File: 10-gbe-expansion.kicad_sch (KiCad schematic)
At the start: 4 parts

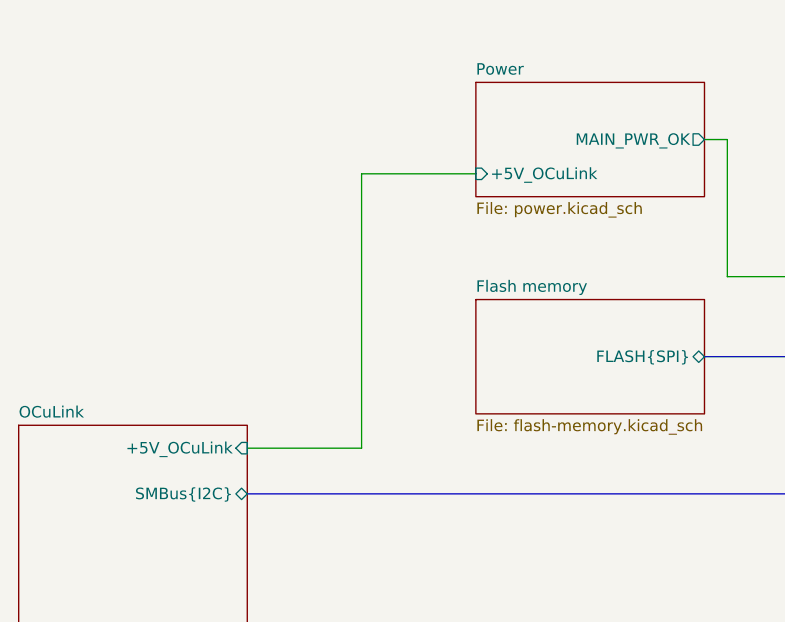
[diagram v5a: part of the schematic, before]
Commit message: [#80813] Remove OCuLink power pins connections
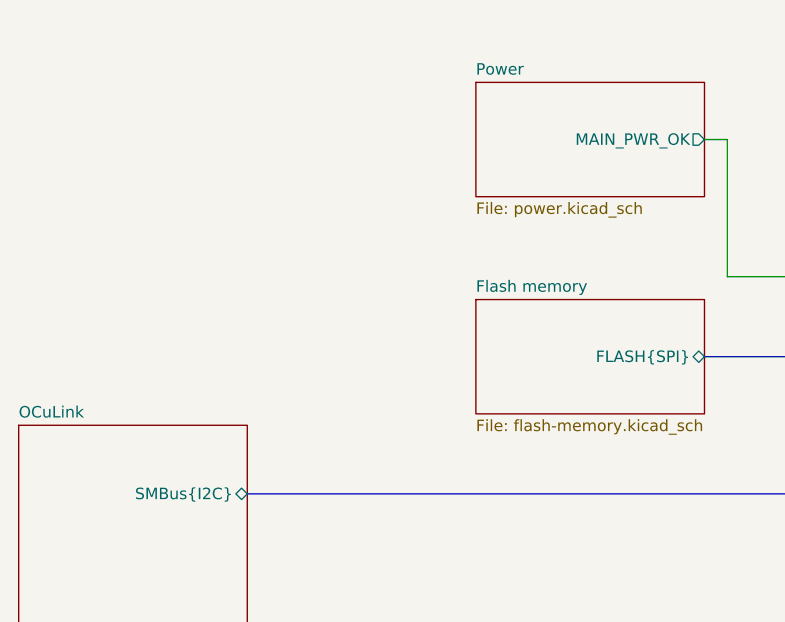
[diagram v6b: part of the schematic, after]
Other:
- sheet OCuLink ports: added none; removed +5V_OCuLink
- sheet Power ports: added none; removed +5V_OCuLink
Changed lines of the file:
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@@
-		)
-	)
-	(wire
-		(pts
-			(xy 88.9 99.06) (xy 88.9 129.54)
-		)
-		(stroke
-			(width 0)
-			(type default)
 		)
 	)
@@
 	(wire
 		(pts
-			(xy 101.6 99.06) (xy 88.9 99.06)
-		)
-		(stroke
-			(width 0)
-			(type default)
-		)
-	)
-	(wire
-		(pts
 			(xy 152.4 110.49) (xy 129.54 110.49)
 		)
@@
 		(pts
 			(xy 279.4 121.92) (xy 304.8 121.92)
-		)
-		(stroke
-			(width 0)
-			(type default)
-		)
-	)
-	(wire
-		(pts
-			(xy 88.9 129.54) (xy 76.2 129.54)
 		)
 		(stroke
@@
 			)
 		)
-		(pin "+5V_OCuLink" input
-			(at 76.2 129.54 0)
-			(effects
-				(font
-					(size 1.27 1.27)
-				)
-				(justify right)
-			)
-		)
 		(pin "~{CPRSNT}" input
 			(at 76.2 157.48 0)
@@
 			)
 		)
-		(pin "+5V_OCuLink" input
-			(at 101.6 99.06 180)
-			(effects
-				(font
-					(size 1.27 1.27)
-				)
-				(justify left)
-			)
-		)
